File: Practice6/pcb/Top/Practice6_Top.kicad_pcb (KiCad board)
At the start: 2 copper layers, 61.5 x 42.5 mm, 14 parts, among them SW1 SW_2, SW2 SW_2, SW3 SW_4, SW4 SW_6, SW5 SW_8, SW6 SW_0

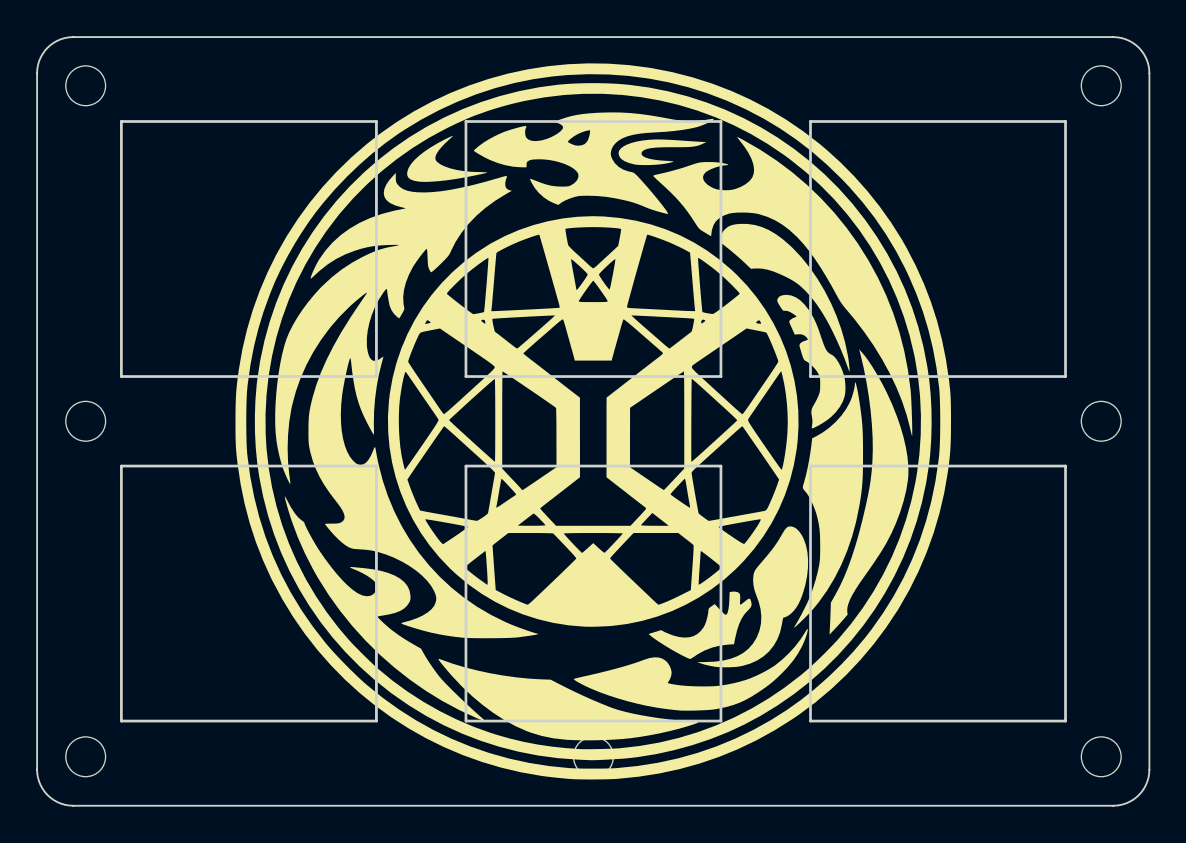
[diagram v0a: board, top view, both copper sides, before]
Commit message: feat: remove silkscreen
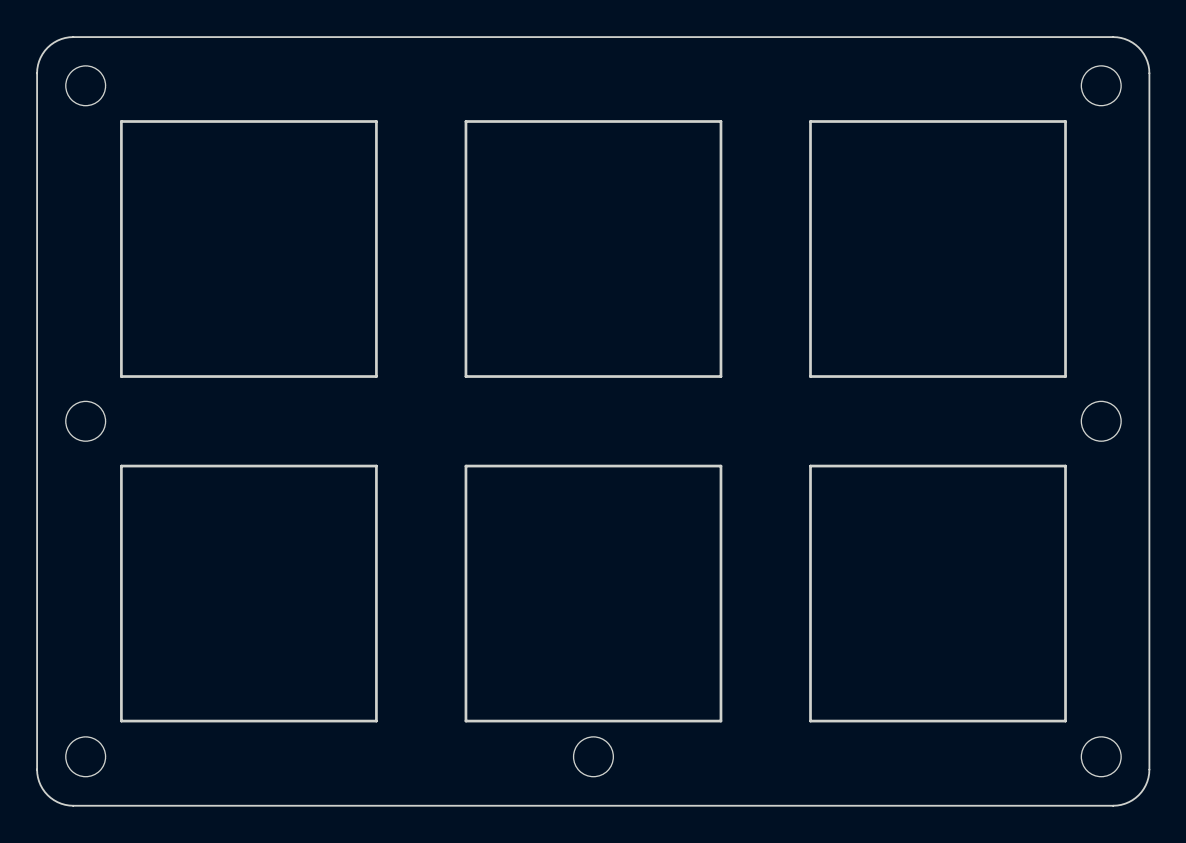
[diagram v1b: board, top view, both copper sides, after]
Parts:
- removed G***: LOGO, Silk_Wizard_logos:silk_wizard_logo_40x40
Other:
- board text removed: "Hurricane6 ver1.0 @Top Designed by multifeb13"
